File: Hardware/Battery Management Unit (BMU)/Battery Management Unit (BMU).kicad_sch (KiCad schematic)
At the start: 16 parts, among them J1 HIGH SIDE, J10 SHUNT, J2 LOW SIDE, J3 POWER, J4 GPIO, J5 5V, J6 3V3, J7 GND, J8 pin header, J9 CAN

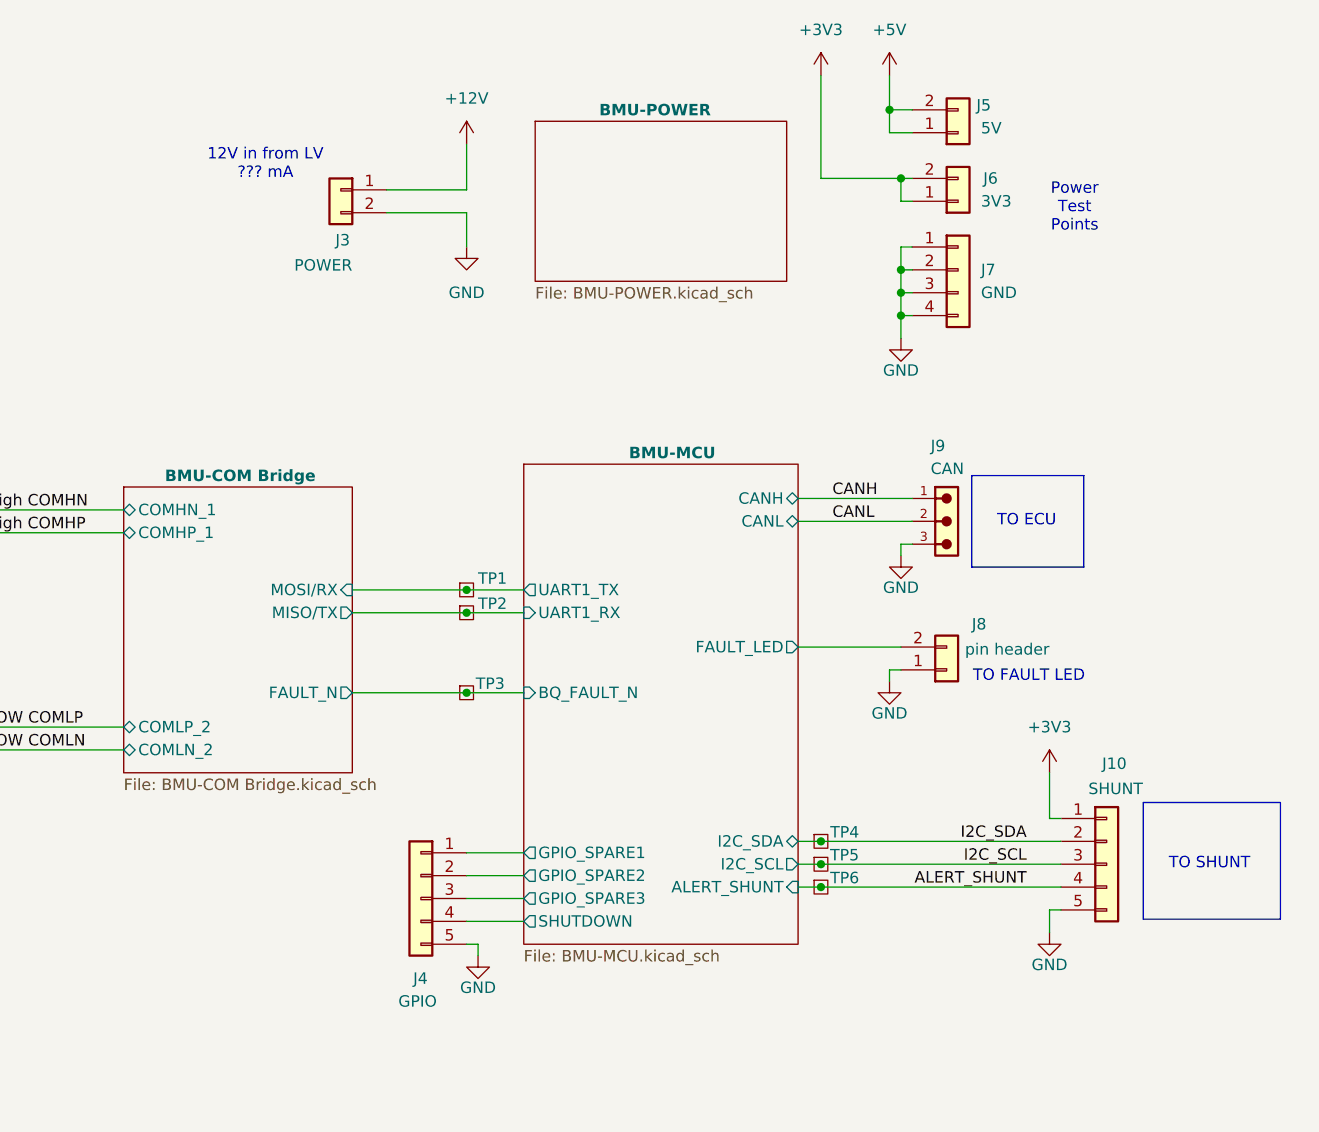
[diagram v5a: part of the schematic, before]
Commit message: doubled up pin for bmu
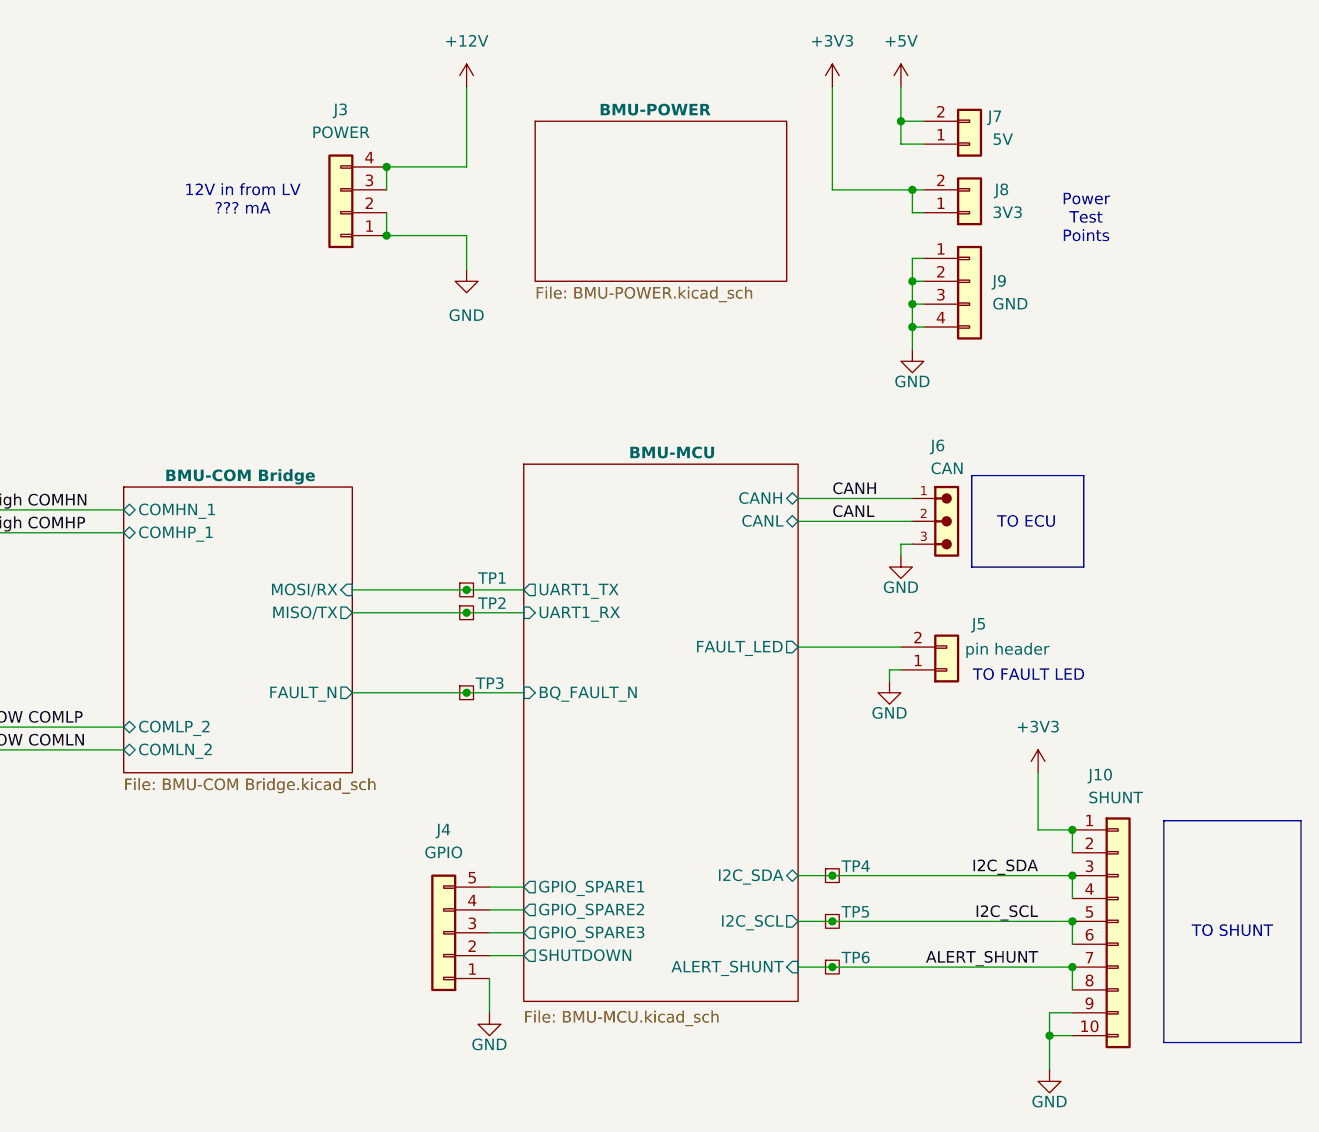
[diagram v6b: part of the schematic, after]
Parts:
- removed J10: SHUNT, Connector_PinHeader_2.54mm:PinHeader_1x05_P2.54mm_Vertical, symbol Connector_Generic:Conn_01x05
- removed J3: POWER, Connector_PinHeader_2.54mm:PinHeader_1x02_P2.54mm_Vertical, symbol Connector_Generic:Conn_01x02
- added J10: SHUNT, Connector_PinHeader_2.54mm:PinHeader_1x10_P2.54mm_Vertical, symbol Connector_Generic:Conn_01x10
- added J3: POWER, Connector_PinHeader_2.54mm:PinHeader_1x04_P2.54mm_Vertical, symbol Connector_Generic:Conn_01x04
- renumbered J8 to J5, J9 to J6, J5 to J7, J6 to J8, J7 to J9
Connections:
- net +12V: now also J3.3 (Pin_3), J3.4 (Pin_4)
- net +3V3: now also J10.1 (Pin_1), J10.2 (Pin_2)
- net ALERT_SHUNT: now also J10.7 (Pin_7), J10.8 (Pin_8)
- net BMU-MCU/GPIO_SPARE1: now also J4.5 (Pin_5); no longer J4.1 (Pin_1)
- net BMU-MCU/GPIO_SPARE2: now also J4.4 (Pin_4); no longer J4.2 (Pin_2)
- net BMU-MCU/SHUTDOWN: now also J4.2 (Pin_2); no longer J4.4 (Pin_4)
- net GND: now also J4.1 (Pin_1), J10.10 (Pin_10), J10.9 (Pin_9), J3.1 (Pin_1), J3.2 (Pin_2); no longer J4.5 (Pin_5)
- net I2C_SCL: now also J10.5 (Pin_5), J10.6 (Pin_6)
- net I2C_SDA: now also J10.3 (Pin_3), J10.4 (Pin_4)
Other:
- moved on the sheet: J7, J8, J9, TP4, TP5, TP6

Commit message: finish! update bmu layout+BOM
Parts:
- J1, J2: symbol 705510038:705510038 -> Connector_Generic:Conn_01x04; DIS (none) -> DigiKey; DPN (none) -> WM14059-ND; MFR (none) -> Molex; MPN (none) -> 705510038; Purchase Link (none) -> https://www.digikey.com/en/products/detail/molex/0705510038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
- J10: DIS (none) -> DigiKey; DPN (none) -> S1011EC-10-ND; MFR (none) -> Sullins Connector Solutions; MPN (none) -> PRPC010SAAN-RC; Purchase Link (none) -> https://www.digikey.com/en/products/detail/sullins-connecto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
- J3, J9: DIS (none) -> DigiKey; DPN (none) -> S1011EC-04-ND; MFR (none) -> Sullins Connector Solutions; MPN (none) -> PRPC004SAAN-RC; Purchase Link (none) -> https://www.digikey.com/en/products/detail/sullins-connecto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
- J4: DIS (none) -> DigiKey; DPN (none) -> S1011EC-05-ND; MFR (none) -> Sullins Connector Solutions; MPN (none) -> PRPC005SAAN-RC; Purchase Link (none) -> https://www.digikey.com/en/products/detail/sullins-connecto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
- J5, J7, J8: DIS (none) -> DigiKey; DPN (none) -> S1011EC-02-ND; MFR (none) -> Sullins Connector Solutions; MPN (none) -> PRPC002SAAN-RC; Purchase Link (none) -> https://www.digikey.com/en/products/detail/sullins-connecto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
- J6: DIS (none) -> DigiKey; DPN (none) -> 732-6062-ND; MFR (none) -> Würth Elektronik; MPN (none) -> 6.91382E+11; Purchase Link (none) -> https://www.digikey.com/en/products/detail/w%C3%BCrth-elekt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
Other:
- note added: "12V → 5V → 3.3V"

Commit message: add jumper+ change SW for bmu
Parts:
- J6: MPN 6.91382E+11 -> 691382000003
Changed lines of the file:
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@@
 			)
 		)
-		(property "MPN" "6.91382E+11"
+		(property "MPN" "691382000003 "
 			(at 350.52 135.89 90)
 			(hide yes)
